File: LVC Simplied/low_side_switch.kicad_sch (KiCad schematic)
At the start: 14 parts, among them Q1 IRF9540N, U1 TL431A, U3 LM393

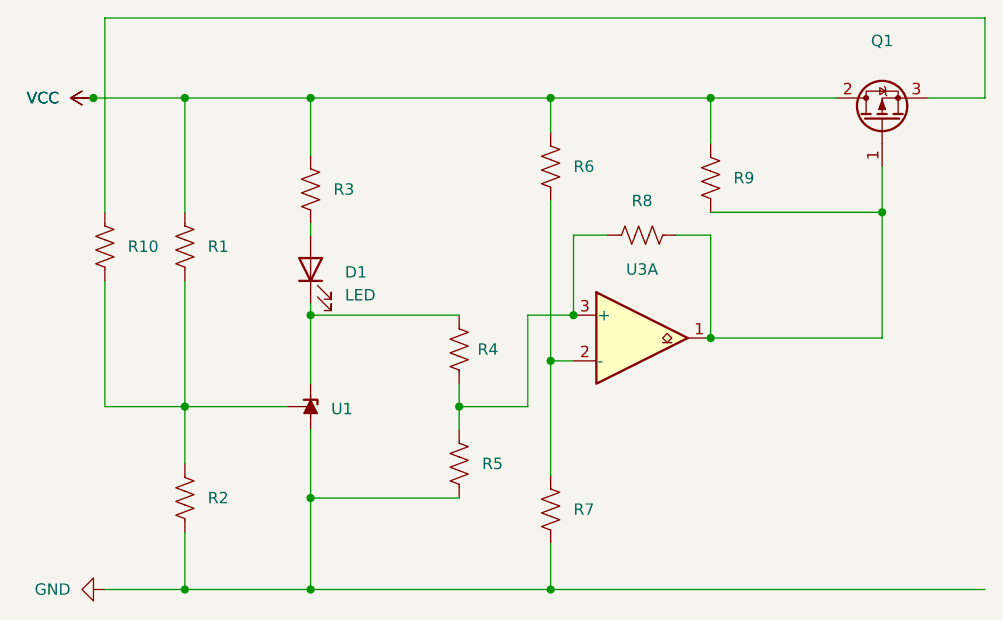
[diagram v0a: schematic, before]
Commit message: LVC Simplified Added
Refining the idea of a simplified LVC circuit and providing two alternatives to doing so.

- High Side Switch
- Low Side Switch (preferred)
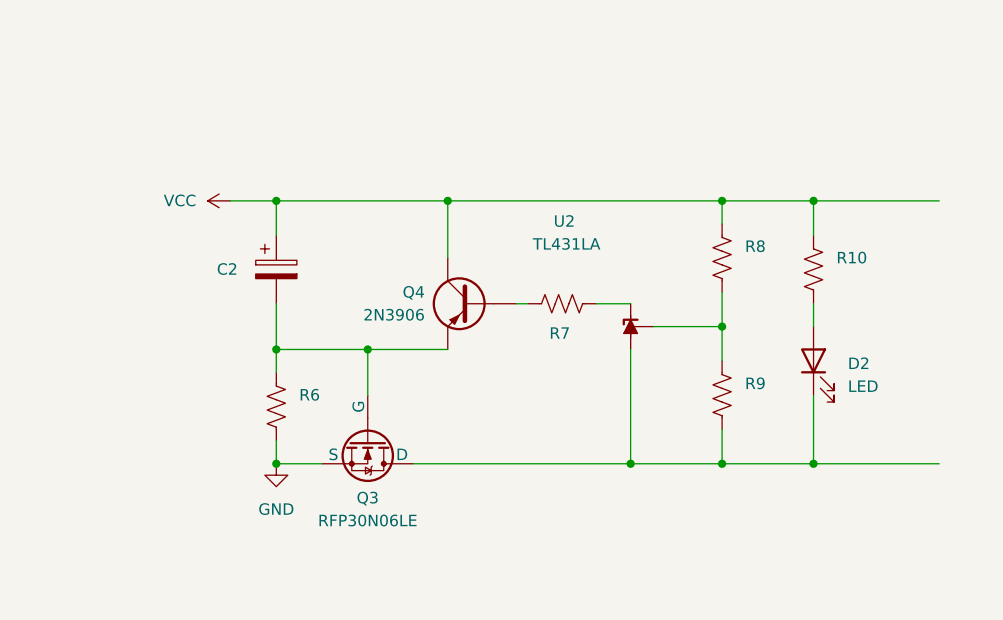
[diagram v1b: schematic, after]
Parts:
- removed D1: LED, symbol Device:LED
- removed Q1: IRF9540N, Package_TO_SOT_THT:TO-220-3_Vertical, symbol Transistor_FET:IRF9540N
- removed R1, R2, R3, R4, R5: R_US, symbol Device:R_US
- removed U1: TL431A, Package_TO_SOT_SMD:SOT-23, symbol Reference_Voltage:TL431DBZ
- removed U3: LM393, symbol Comparator:LM393
- added C2: C_Polarized, symbol Device:C_Polarized
- added D2: LED, symbol Device:LED
- added Q3: RFP30N06LE, symbol Simulation_SPICE:NMOS
- added Q4: 2N3906, Package_TO_SOT_THT:TO-92_Inline, symbol Transistor_BJT:2N3906
- added U2: TL431LA, Package_TO_SOT_THT:TO-92_Inline, symbol Reference_Voltage:TL431LP
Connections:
- net GND: now also R6.2, Q3.3 (S); no longer R7.2
- net VCC: now also R10.1, R8.1, C2.1, Q4.3 (C); no longer R6.1, R9.1
- net at R9.2: now also D2.1 (K), Q3.1 (D), U2.2 (A); no longer R8.2
- net at R10.2: now also D2.2 (A)
- net at R7.1: now also Q4.2 (B); no longer R6.2
- new net: R7.2, U2.3 (K)
- new net: C2.2, Q3.2 (G), Q4.1 (E), R6.1
- new net: R8.2, R9.1, U2.1 (REF)

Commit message: Low Side Switch Updates
Added pull-up resistor between Base and Emitter of 2N3906 to make sure that Base has a clean and definite value when switched off instead of a floating state.
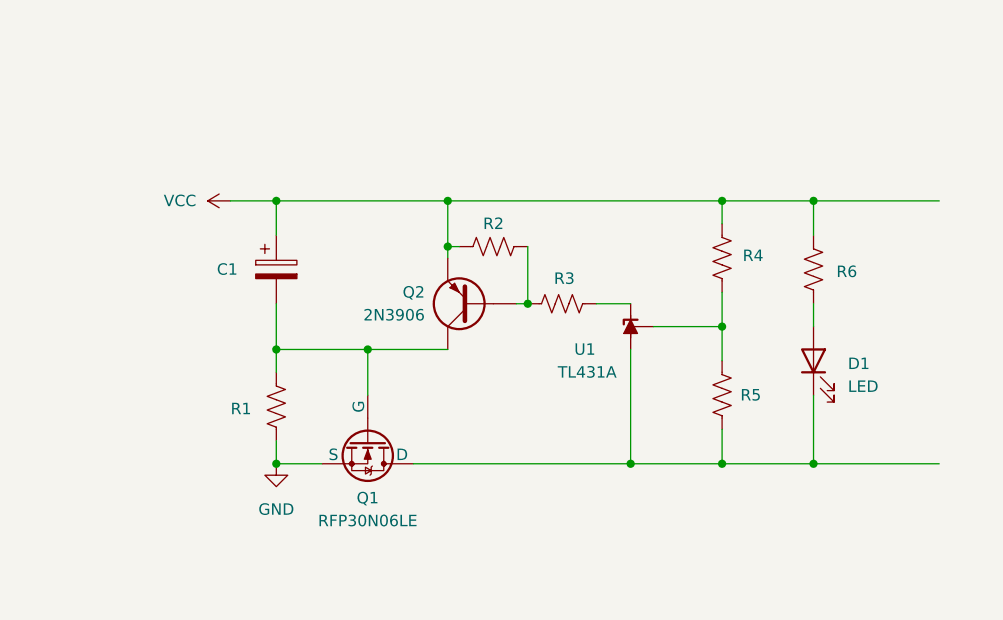
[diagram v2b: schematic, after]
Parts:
- removed Q4: 2N3906, Package_TO_SOT_THT:TO-92_Inline, symbol Transistor_BJT:2N3906
- added Q2: 2N3906, Package_TO_SOT_THT:TO-92_Inline, symbol Transistor_BJT:2N3906
- added R2: R_US, symbol Device:R_US
- U1: renamed from U2; value TL431LA -> TL431A
- renumbered C2 to C1, D2 to D1, Q3 to Q1, R6 to R1, R7 to R3, R8 to R4, R9 to R5, R10 to R6
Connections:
- net VCC: now also Q2.1 (E), R2.1
- net at R3.1: now also Q2.2 (B), R2.2
- net at C1.2, Q1.2 (G), R1.1: now also Q2.3 (C)

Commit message: Low Side Switch Refinements
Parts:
- renumbered C1 to C2, D1 to D2, Q1 to Q3, R6 to R10, R1 to R6, R3 to R7, R4 to R8, R5 to R9, U1 to U2
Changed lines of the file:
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@@
 		(in_pos_files yes)
 		(dnp no)
-		(property "Reference" "R3"
+		(property "Reference" "R7"
 			(at 91.694 55.626 90)
 			(show_name no)
@@
 		(dnp no)
 		(fields_autoplaced yes)
-		(property "Reference" "#PWR01"
+		(property "Reference" "#PWR04"
 			(at 58.42 46.99 0)
 			(hide yes)
@@
 				)
 			)
+			(project "LVC Simplied"
+				(path "/acb6d58f-17eb-46bf-805a-64edbdb6e1b5"
+					(reference "Q2")
+					(unit 1)
+				)
+			)
 		)
 	)
@@
 		(dnp no)
 		(fields_autoplaced yes)
-		(property "Reference" "Q1"
+		(property "Reference" "Q3"
 			(at 69.85 80.01 90)
 			(show_name no)
@@
 		(in_pos_files yes)
 		(dnp no)
-		(property "Reference" "C1"
+		(property "Reference" "C2"
 			(at 53.086 54.61 0)
 			(show_name no)
@@
 		(in_pos_files yes)
 		(dnp no)
-		(property "Reference" "U1"
+		(property "Reference" "U2"
 			(at 93.98 63.5 90)
 			(show_name no)
@@
 		(in_pos_files yes)
 		(dnp no)
-		(property "Reference" "R6"
+		(property "Reference" "R10"
 			(at 121.92 54.864 0)
 			(show_name no)
@@
 		(in_pos_files yes)
 		(dnp no)
-		(property "Reference" "R1"
+		(property "Reference" "R6"
 			(at 54.61 70.104 0)
 			(show_name no)
@@
 		(in_pos_files yes)
 		(dnp no)
-		(property "Reference" "R4"
+		(property "Reference" "R8"
 			(at 111.506 53.086 0)
 			(show_name no)
@@
 		(dnp no)
 		(fields_autoplaced yes)
-		(property "Reference" "D1"
+		(property "Reference" "D2"
 			(at 123.19 65.0874 90)
 			(show_name no)
@@
 				)
 			)
+			(project "LVC Simplied"
+				(path "/acb6d58f-17eb-46bf-805a-64edbdb6e1b5"
+					(reference "R2")
+					(unit 1)
+				)
+			)
 		)
 	)
@@
 		(in_pos_files yes)
 		(dnp no)
-		(property "Reference" "R5"
+		(property "Reference" "R9"
 			(at 111.252 68.58 0)
 			(show_name no)
@@
 		)
 	)
-	(embedded_fonts no)
 )

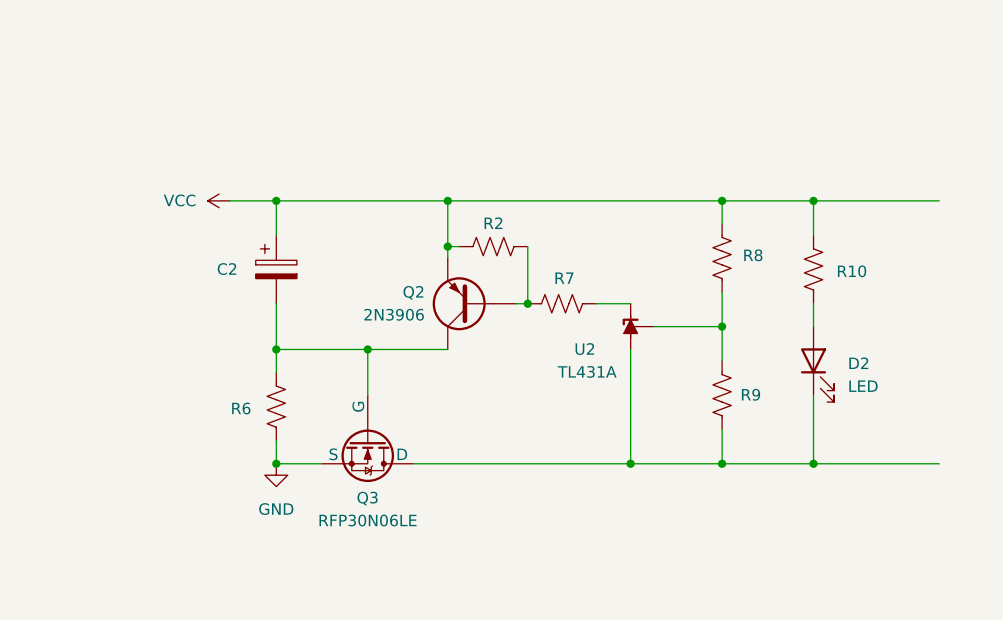
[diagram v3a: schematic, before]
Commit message: LVC Low Side V2
Another version of a low side switch is provided that has the following features:

- Way lower power consumption
- A blinking LED that provides a visual indication that the power is past the cutt_off point
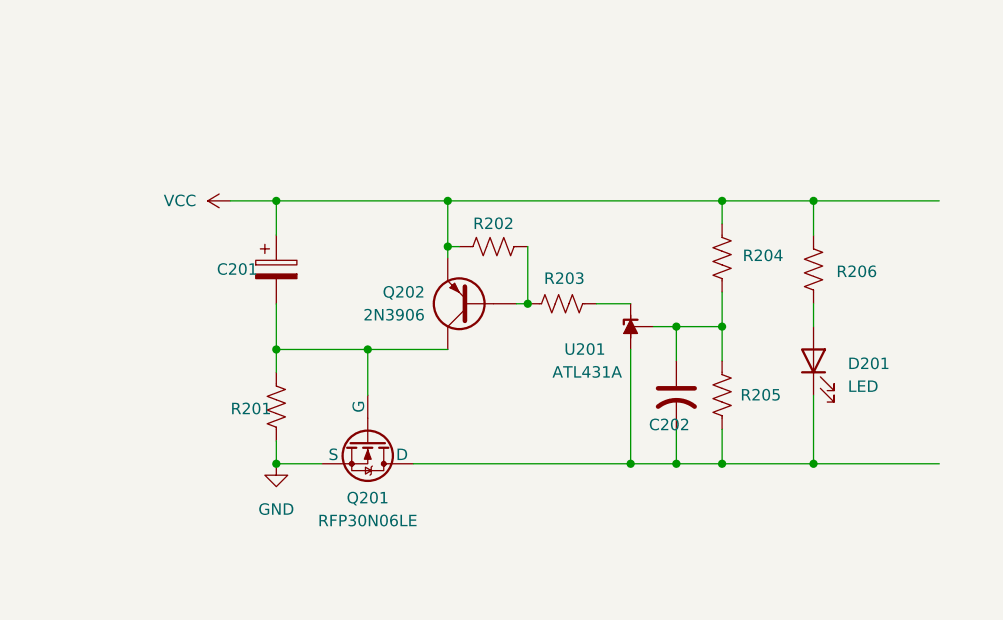
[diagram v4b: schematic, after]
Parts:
- added C202: C_US, symbol Device:C_US
- U201: renamed from U2; value TL431A -> ATL431A
- renumbered C2 to C201, D2 to D201, Q3 to Q201, Q2 to Q202, R6 to R201, R2 to R202, R7 to R203, R8 to R204, R9 to R205, R10 to R206
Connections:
- net at D201.1 (K), Q201.1 (D), R205.2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: now also C202.2
- net at R204.2, R205.1, U201.1 (REF): now also C202.1
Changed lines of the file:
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@@
+	)
+	(junction
+		(at 104.14 60.96)
+		(diameter 0)
+		(color 0 0 0 0)
 	)
 	(junction
@@
 	)
 	(junction
+		(at 104.14 76.2)
+		(diameter 0)
+		(color 0 0 0 0)
+	)
+	(junction
 		(at 78.74 46.99)
 		(diameter 0)
@@
 	(wire
 		(pts
-			(xy 99.06 76.2) (xy 109.22 76.2)
+			(xy 99.06 76.2) (xy 104.14 76.2)
 		)
 		(stroke
@@
 	(wire
 		(pts
+			(xy 104.14 72.39) (xy 104.14 76.2)
+		)
+		(stroke
+			(width 0)
+			(type default)
+		)
+	)
+	(wire
+		(pts
 			(xy 119.38 46.99) (xy 119.38 50.8)
 		)
@@
 	(wire
 		(pts
+			(xy 104.14 76.2) (xy 109.22 76.2)
+		)
+		(stroke
+			(width 0)
+			(type default)
+		)
+	)
+	(wire
+		(pts
 			(xy 59.69 46.99) (xy 78.74 46.99)
 		)
@@
 	(wire
 		(pts
+			(xy 104.14 60.96) (xy 104.14 64.77)
+		)
+		(stroke
+			(width 0)
+			(type default)
+		)
+	)
+	(wire
+		(pts
+			(xy 104.14 60.96) (xy 109.22 60.96)
+		)
+		(stroke
+			(width 0)
+			(type default)
+		)
+	)
+	(wire
+		(pts
 			(xy 99.06 63.5) (xy 99.06 76.2)
 		)
@@
 	(wire
 		(pts
-			(xy 101.6 60.96) (xy 109.22 60.96)
+			(xy 101.6 60.96) (xy 104.14 60.96)
 		)
 		(stroke
@@
 		(in_pos_files yes)
 		(dnp no)
-		(property "Reference" "R7"
+		(property "Reference" "R203"
 			(at 91.694 55.626 90)
 			(show_name no)
@@
 			(project "LVC Simplied"
 				(path "/acb6d58f-17eb-46bf-805a-64edbdb6e1b5"
-					(reference "R7")
+					(reference "R203")
 					(unit 1)
 				)
@@
 		(dnp no)
 		(fields_autoplaced yes)
-		(property "Reference" "#PWR04"
+		(property "Reference" "#PWR0201"
 			(at 58.42 46.99 0)
 			(hide yes)
@@
 			(project "LVC Simplied"
 				(path "/acb6d58f-17eb-46bf-805a-64edbdb6e1b5"
-					(reference "#PWR04")
+					(reference "#PWR0201")
 					(unit 1)
 				)
@@
 		(dnp no)
 		(fields_autoplaced yes)
-		(property "Reference" "Q2"
+		(property "Reference" "Q202"
 			(at 76.2 57.1499 0)
 			(show_name no)
@@
 			(project "LVC Simplied"
 				(path "/acb6d58f-17eb-46bf-805a-64edbdb6e1b5"
-					(reference "Q2")
+					(reference "Q202")
 					(unit 1)
 				)
@@
 		(dnp no)
 		(fields_autoplaced yes)
-		(property "Reference" "Q3"
+		(property "Reference" "Q201"
 			(at 69.85 80.01 90)
 			(show_name no)
@@
 			(project "LVC Simplied"
 				(path "/acb6d58f-17eb-46bf-805a-64edbdb6e1b5"
-					(reference "Q3")
+					(reference "Q201")
 					(unit 1)
 				)
@@
 		(in_pos_files yes)
 		(dnp no)
-		(property "Reference" "C2"
+		(property "Reference" "C201"
 			(at 53.086 54.61 0)
 			(show_name no)
@@
 			(project "LVC Simplied"
 				(path "/acb6d58f-17eb-46bf-805a-64edbdb6e1b5"
-					(reference "C2")
+					(reference "C201")
 					(unit 1)
 				)
@@
 		(in_pos_files yes)
 		(dnp no)
-		(property "Reference" "U2"
+		(property "Reference" "U201"
 			(at 93.98 63.5 90)
 			(show_name no)
@@
 			)
 		)
-		(property "Value" "TL431A"
+		(property "Value" "ATL431A"
 			(at 94.234 66.04 90)
 			(show_name no)
@@
 			(project "LVC Simplied"
 				(path "/acb6d58f-17eb-46bf-805a-64edbdb6e1b5"
-					(reference "U2")
+					(reference "U201")
 					(unit 1)
 				)
@@
 		(dnp no)
 		(fields_autoplaced yes)
-		(property "Reference" "#PWR02"
+		(property "Reference" "#PWR0202"
 			(at 59.69 82.55 0)
 			(hide yes)
@@
 			(project "LVC Simplied"
 				(path "/acb6d58f-17eb-46bf-805a-64edbdb6e1b5"
-					(reference "#PWR02")
+					(reference "#PWR0202")
 					(unit 1)
 				)
@@
 		(in_pos_files yes)
 		(dnp no)
-		(property "Reference" "R10"
+		(property "Reference" "R206"
 			(at 121.92 54.864 0)
 			(show_name no)
@@
 			(project "LVC Simplied"
 				(path "/acb6d58f-17eb-46bf-805a-64edbdb6e1b5"
-					(reference "R10")
+					(reference "R206")
 					(unit 1)
 				)
@@
 		(in_pos_files yes)
 		(dnp no)
-		(property "Reference" "R6"
+		(property "Reference" "R201"
 			(at 54.61 70.104 0)
 			(show_name no)
@@
 			(project "LVC Simplied"
 				(path "/acb6d58f-17eb-46bf-805a-64edbdb6e1b5"
-					(reference "R6")
+					(reference "R201")
 					(unit 1)
 				)
@@
 		(in_pos_files yes)
 		(dnp no)
-		(property "Reference" "R8"
+		(property "Reference" "R204"
 			(at 111.506 53.086 0)
 			(show_name no)
@@
 			(project "LVC Simplied"
 				(path "/acb6d58f-17eb-46bf-805a-64edbdb6e1b5"
-					(reference "R8")
+					(reference "R204")
+					(unit 1)
+				)
+			)
+		)
+	)
+	(symbol
+		(lib_id "Device:C_US")
+		(at 104.14 68.58 0)
+		(unit 1)
+		(body_style 1)
+		(exclude_from_sim no)
+		(in_bom yes)
+		(on_board yes)
+		(in_pos_files yes)
+		(dnp no)
+		(property "Reference" "C202"
+			(at 101.092 71.882 0)
+			(show_name no)
+			(do_not_autoplace no)
+			(effects
+				(font
+					(size 1.27 1.27)
+				)
+				(justify left)
+			)
+		)
+		(property "Value" "C_US"
+			(at 107.95 70.1039 0)
+			(hide yes)
+			(show_name no)
+			(do_not_autoplace no)
+			(effects
+				(font
+					(size 1.27 1.27)
+				)
+				(justify left)
+			)
+		)
+		(property "Footprint" ""
+			(at 104.14 68.58 0)
+			(hide yes)
+			(show_name no)
+			(do_not_autoplace no)
+			(effects
+				(font
+					(size 1.27 1.27)
+				)
+			)
+		)
+		(property "Datasheet" ""
+			(at 104.14 68.58 0)
+			(hide yes)
+			(show_name no)
+			(do_not_autoplace no)
+			(effects
+				(font
+					(size 1.27 1.27)
+				)
+			)
+		)
+		(property "Description" "capacitor, US symbol"
+			(at 104.14 68.58 0)
+			(hide yes)
+			(show_name no)
+			(do_not_autoplace no)
+			(effects
+				(font
+					(size 1.27 1.27)
+				)
+			)
+		)
+		(pin "2"
+		)
+		(pin "1"
+		)
+		(instances
+			(project "low_side_switch"
+				(path "/7112f0df-75c9-4e64-bf70-7a1c84de0c11"
+					(reference "C2")
+					(unit 1)
+				)
+			)
+			(project "LVC Simplied"
+				(path "/acb6d58f-17eb-46bf-805a-64edbdb6e1b5"
+					(reference "C202")
 					(unit 1)
 				)
@@
 		(dnp no)
 		(fields_autoplaced yes)
-		(property "Reference" "D2"
+		(property "Reference" "D201"
 			(at 123.19 65.0874 90)
 			(show_name no)
@@
 			(project "LVC Simplied"
 				(path "/acb6d58f-17eb-46bf-805a-64edbdb6e1b5"
-					(reference "D2")
+					(reference "D201")
 					(unit 1)
 				)
@@
 		(in_pos_files yes)
 		(dnp no)
-		(property "Reference" "R2"
+		(property "Reference" "R202"
 			(at 83.82 49.53 90)
 			(show_name no)
@@
 			(project "LVC Simplied"
 				(path "/acb6d58f-17eb-46bf-805a-64edbdb6e1b5"
-					(reference "R2")
+					(reference "R202")
 					(unit 1)
 				)
@@
 		(in_pos_files yes)
 		(dnp no)
-		(property "Reference" "R9"
+		(property "Reference" "R205"
 			(at 111.252 68.58 0)
 			(show_name no)
@@
 			(project "LVC Simplied"
 				(path "/acb6d58f-17eb-46bf-805a-64edbdb6e1b5"
-					(reference "R9")
-					(unit 1)
-				)
+					(reference "R205")
+					(unit 1)
+				)
